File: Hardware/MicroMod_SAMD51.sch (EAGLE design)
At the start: 30 parts, among them J2 MICROMOD-2222, U1 W25QXX128MBIT-6X5-NO_CENTER, U2 ATSAMD51J20A-A, Y1 32.768kHz

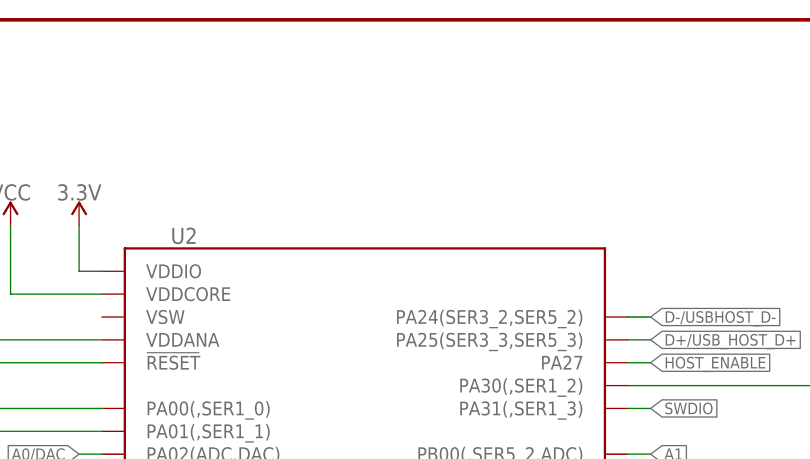
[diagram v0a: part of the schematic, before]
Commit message: Adds voltage range to schematic
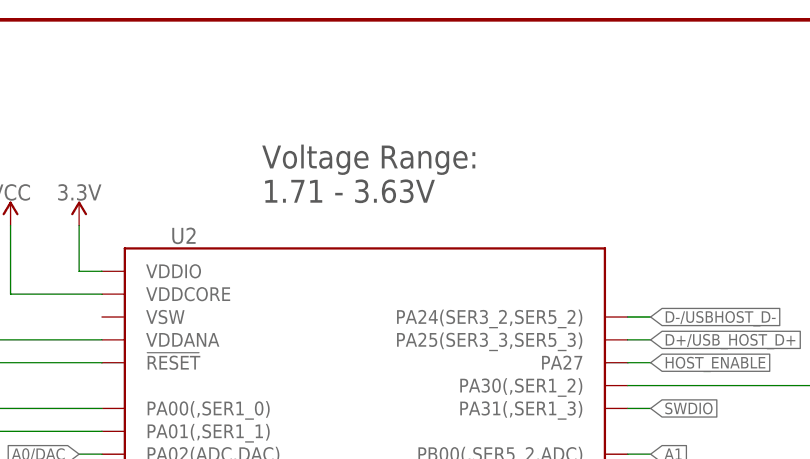
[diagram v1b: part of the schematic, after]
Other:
- note added: "Voltage Range: 1.71 - 3.63V"
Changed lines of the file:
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@@
 <text x="285.496" y="242.062" size="1.778" layer="97" font="vector">0.65uA Leakage
 0.3V drop at 10mA</text>
+<text x="106.68" y="259.08" size="2.54" layer="97" font="vector">Voltage Range:
+1.71 - 3.63V</text>
 </plain>
 <instances>

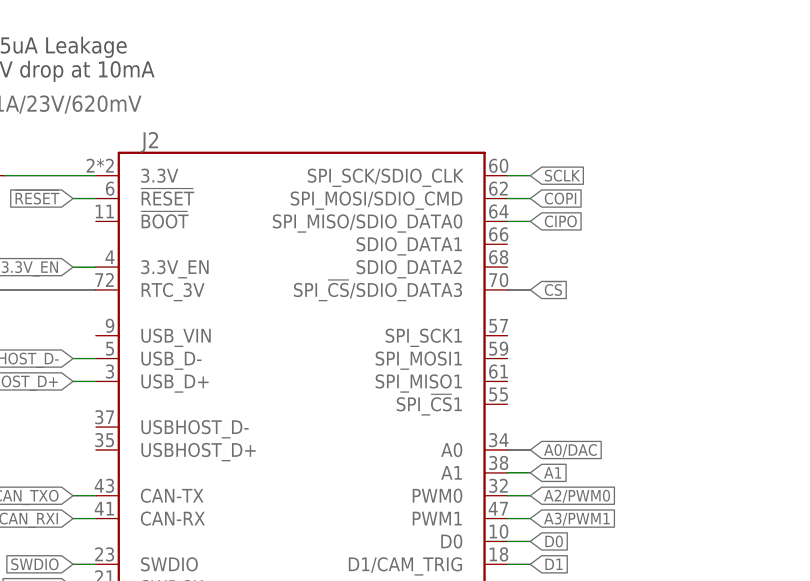
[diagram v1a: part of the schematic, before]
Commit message: Updates the micromodd connector and swaps the SPI pins
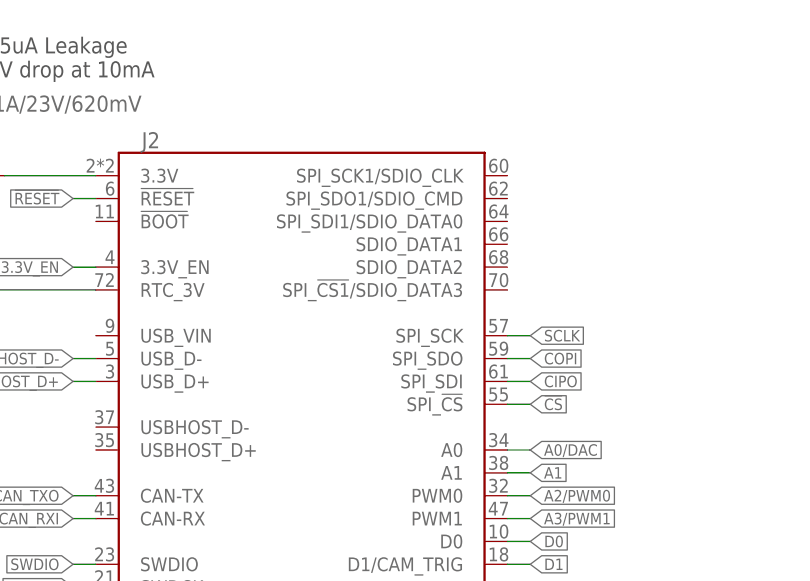
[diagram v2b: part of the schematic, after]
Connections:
- net !CS: now also J2.SPI_!CS!; no longer J2.SPI_!CS!/SDIO_DATA3
- net CIPO: now also J2.SPI_SDI; no longer J2.SPI_MISO/SDIO_DATA0
- net COPI: now also J2.SPI_SDO; no longer J2.SPI_MOSI/SDIO_CMD
- net SCLK: now also J2.SPI_SCK; no longer J2.SPI_SCK/SDIO_CLK
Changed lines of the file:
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@@
 </segment>
 <segment>
-<pinref part="J2" gate="J1" pin="SPI_MOSI/SDIO_CMD"/>
-<wire x1="345.44" y1="228.6" x2="347.98" y2="228.6" width="0.1524" layer="91"/>
-<label x="347.98" y="228.6" size="1.27" layer="95" xref="yes"/>
+<pinref part="J2" gate="J1" pin="SPI_SDO"/>
+<wire x1="345.44" y1="210.82" x2="347.98" y2="210.82" width="0.1524" layer="91"/>
+<label x="347.98" y="210.82" size="1.27" layer="95" xref="yes"/>
 </segment>
 </net>
 <net name="CIPO" class="0">
 <segment>
-<pinref part="J2" gate="J1" pin="SPI_MISO/SDIO_DATA0"/>
-<wire x1="345.44" y1="226.06" x2="347.98" y2="226.06" width="0.1524" layer="91"/>
-<label x="347.98" y="226.06" size="1.27" layer="95" xref="yes"/>
-</segment>
-<segment>
 <wire x1="88.9" y1="220.98" x2="86.36" y2="220.98" width="0.1524" layer="91"/>
 <label x="86.36" y="220.98" size="1.27" layer="95" font="vector" rot="R180" xref="yes"/>
 <pinref part="U2" gate="G$1" pin="PA06(,SER0_2,ADC,VREFC)"/>
+</segment>
+<segment>
+<pinref part="J2" gate="J1" pin="SPI_SDI"/>
+<wire x1="345.44" y1="208.28" x2="347.98" y2="208.28" width="0.1524" layer="91"/>
+<label x="347.98" y="208.28" size="1.27" layer="95" xref="yes"/>
 </segment>
 </net>
@@
 <net name="SCLK" class="1">
 <segment>
-<pinref part="J2" gate="J1" pin="SPI_SCK/SDIO_CLK"/>
-<wire x1="345.44" y1="231.14" x2="347.98" y2="231.14" width="0.1524" layer="91"/>
-<label x="347.98" y="231.14" size="1.27" layer="95" xref="yes"/>
-</segment>
-<segment>
 <wire x1="88.9" y1="223.52" x2="86.36" y2="223.52" width="0.1524" layer="91"/>
 <label x="86.36" y="223.52" size="1.27" layer="95" font="vector" rot="R180" xref="yes"/>
 <pinref part="U2" gate="G$1" pin="PA05(,SER0_1,ADC,DAC)"/>
+</segment>
+<segment>
+<pinref part="J2" gate="J1" pin="SPI_SCK"/>
+<wire x1="345.44" y1="213.36" x2="347.98" y2="213.36" width="0.1524" layer="91"/>
+<label x="347.98" y="213.36" size="1.27" layer="95" xref="yes"/>
 </segment>
 </net>
@@
 </segment>
 <segment>
-<pinref part="J2" gate="J1" pin="SPI_!CS!/SDIO_DATA3"/>
-<wire x1="345.44" y1="218.44" x2="347.98" y2="218.44" width="0.1524" layer="91"/>
-<label x="347.98" y="218.44" size="1.27" layer="95" xref="yes"/>
+<pinref part="J2" gate="J1" pin="SPI_!CS!"/>
+<wire x1="345.44" y1="205.74" x2="347.98" y2="205.74" width="0.1524" layer="91"/>
+<label x="347.98" y="205.74" size="1.27" layer="95" xref="yes"/>
 </segment>
 </net>

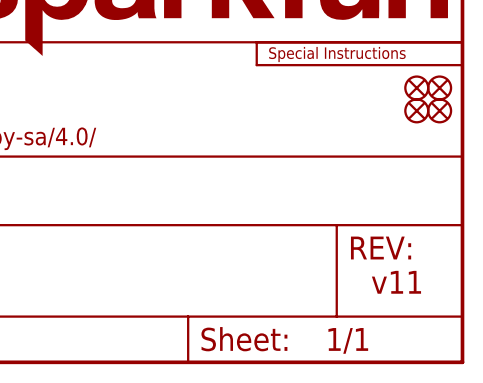
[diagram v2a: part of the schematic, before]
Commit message: Fixes LED assignment in variant,  routes SPI lines, rolls version to v12
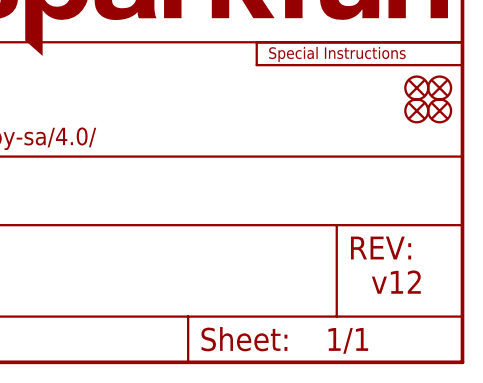
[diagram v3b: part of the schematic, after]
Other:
- note added: "v12"
- note removed: "v11"
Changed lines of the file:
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@@
 <sheet>
 <plain>
-<text x="421.64" y="7.62" size="2.54" layer="94" font="vector">v11</text>
+<text x="421.64" y="7.62" size="2.54" layer="94" font="vector">v12</text>
 <text x="250.64" y="273.78" size="2.54" layer="94" font="vector" align="center">M.2 Connector</text>
 <wire x1="231.14" y1="279.4" x2="231.14" y2="111.76" width="0.1524" layer="97" style="longdash"/>

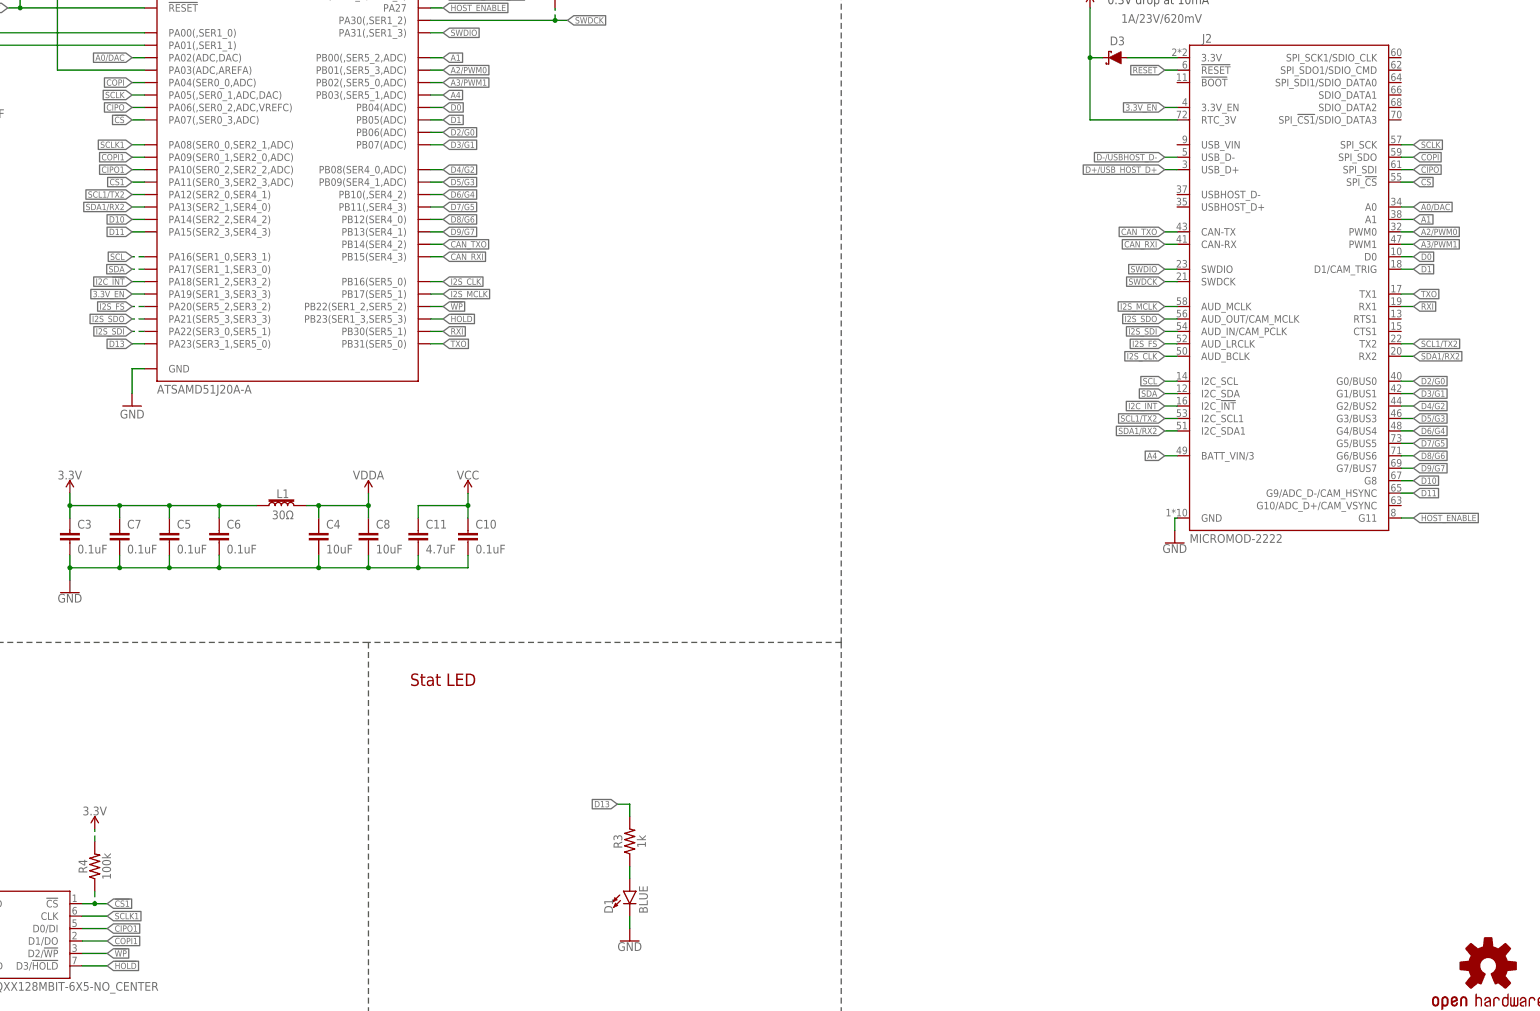
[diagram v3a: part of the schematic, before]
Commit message: Updates SPI clock names to correct abbreviation
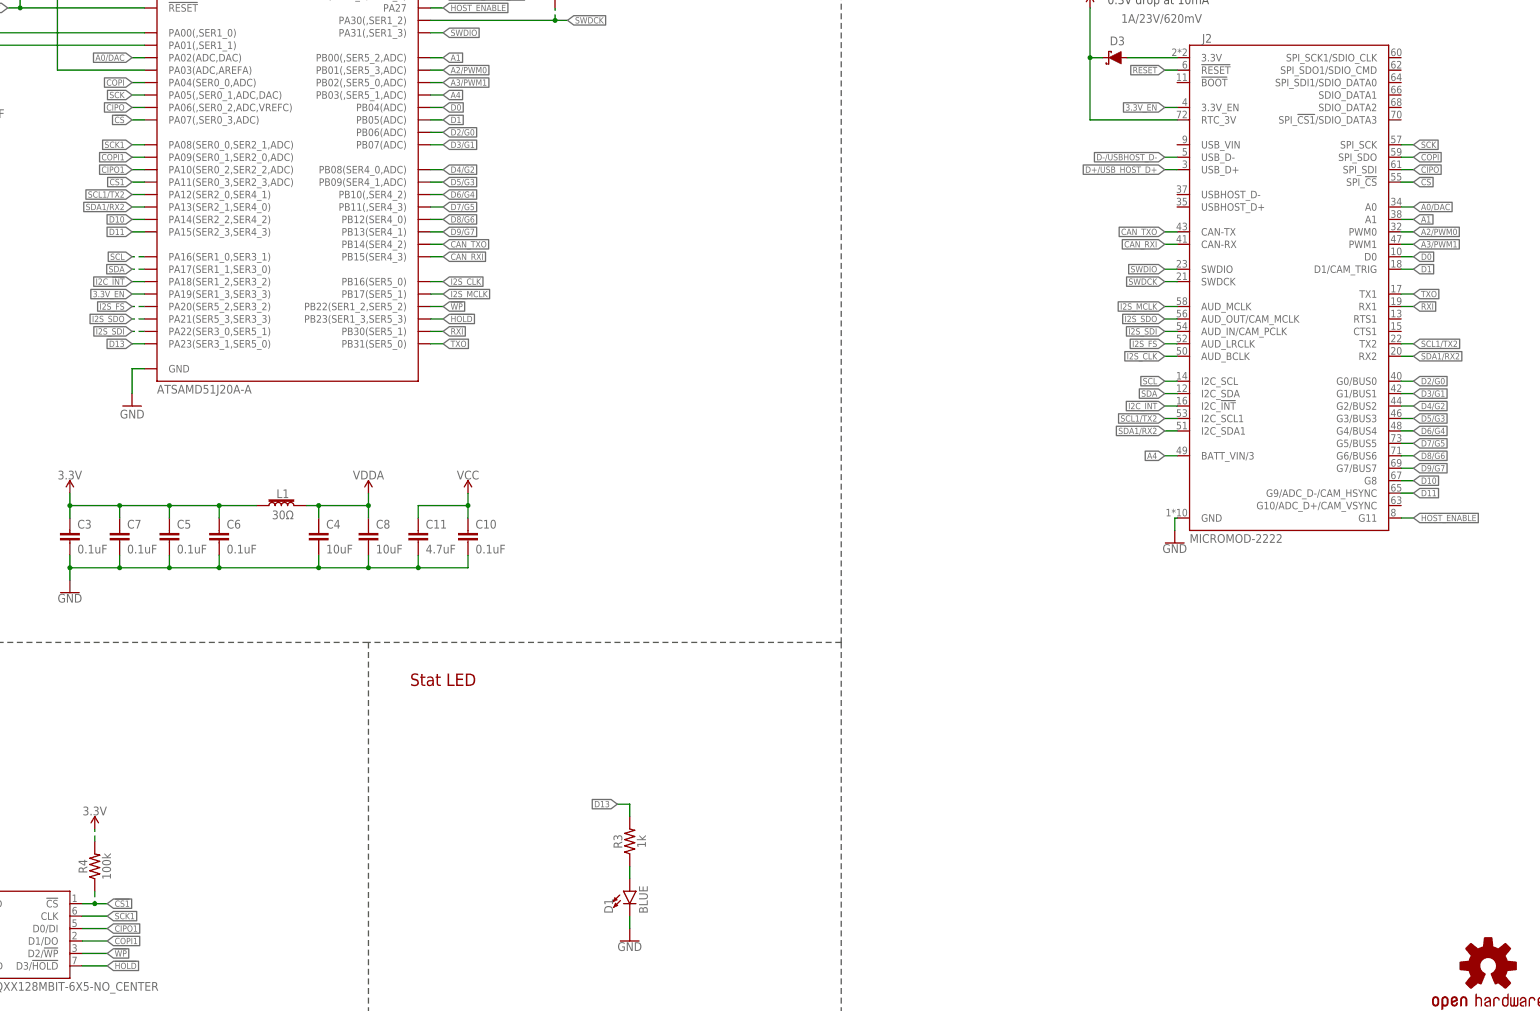
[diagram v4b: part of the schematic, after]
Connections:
- net SCLK renamed SCK
- net SCLK1 renamed SCK1
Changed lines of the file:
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@@
 </segment>
 </net>
-<net name="SCLK" class="1">
+<net name="SCK" class="1">
 <segment>
 <wire x1="88.9" y1="223.52" x2="86.36" y2="223.52" width="0.1524" layer="91"/>
@@
 </segment>
 </net>
-<net name="SCLK1" class="1">
+<net name="SCK1" class="1">
 <segment>
 <pinref part="U1" gate="U1" pin="CLK"/>

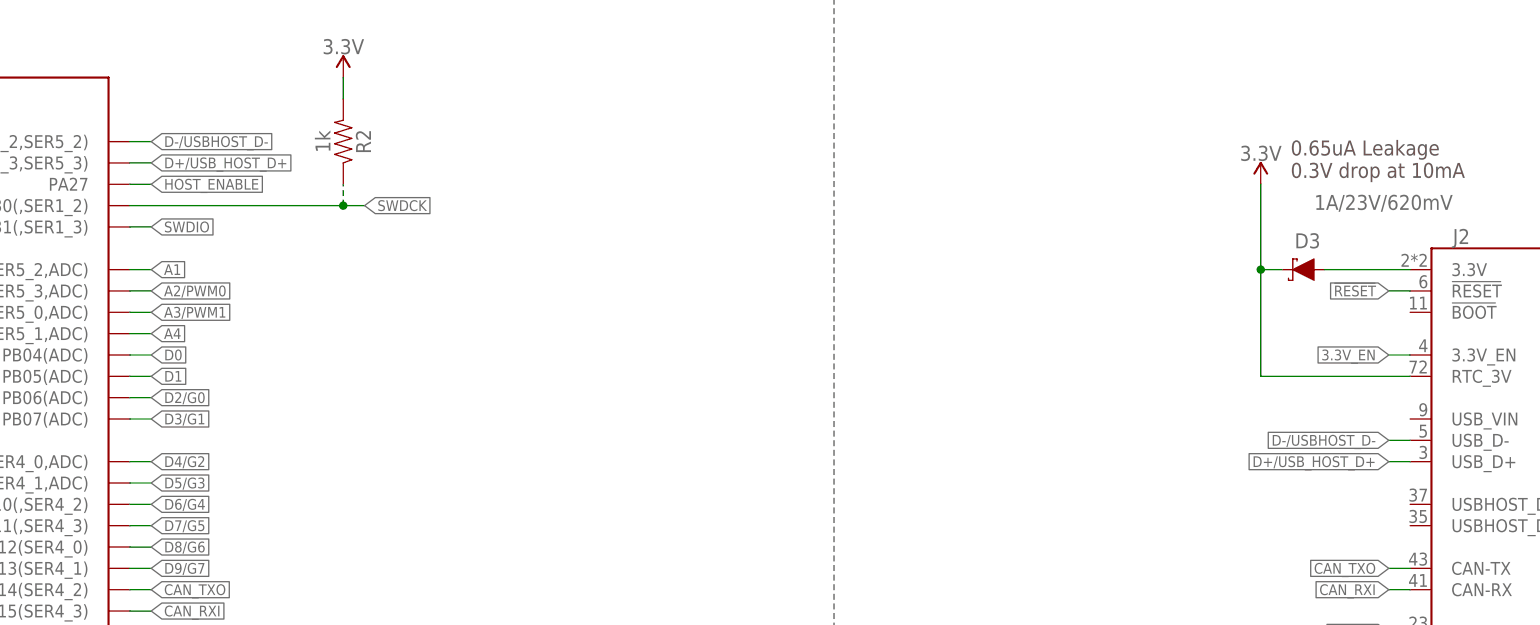
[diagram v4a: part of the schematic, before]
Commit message: Fixes typo in usbhost_D+ net
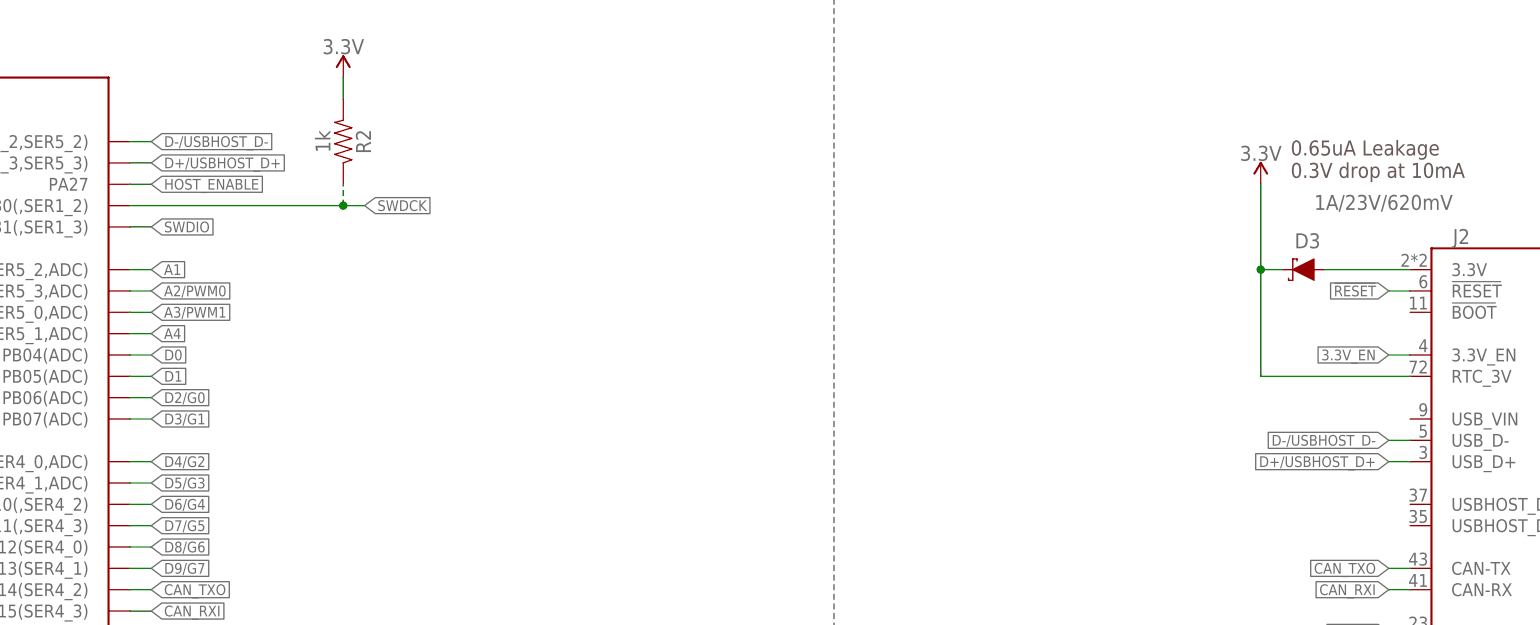
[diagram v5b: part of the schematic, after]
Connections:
- net D+/USB_HOST_D+ renamed D+/USBHOST_D+
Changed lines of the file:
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@@
 </segment>
 </net>
-<net name="D+/USB_HOST_D+" class="2">
+<net name="D+/USBHOST_D+" class="2">
 <segment>
 <pinref part="J2" gate="J1" pin="USB_D+"/>

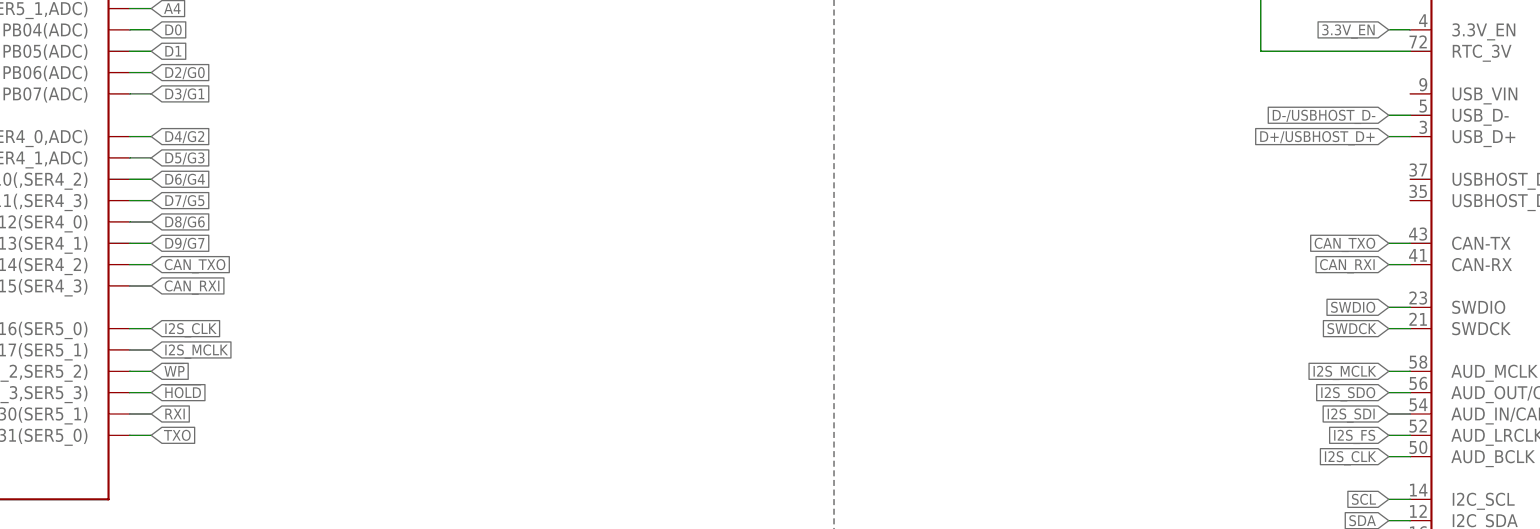
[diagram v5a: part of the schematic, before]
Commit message: Updates CAN net names - CAN is not supported on SAM-"D" versions of the IC
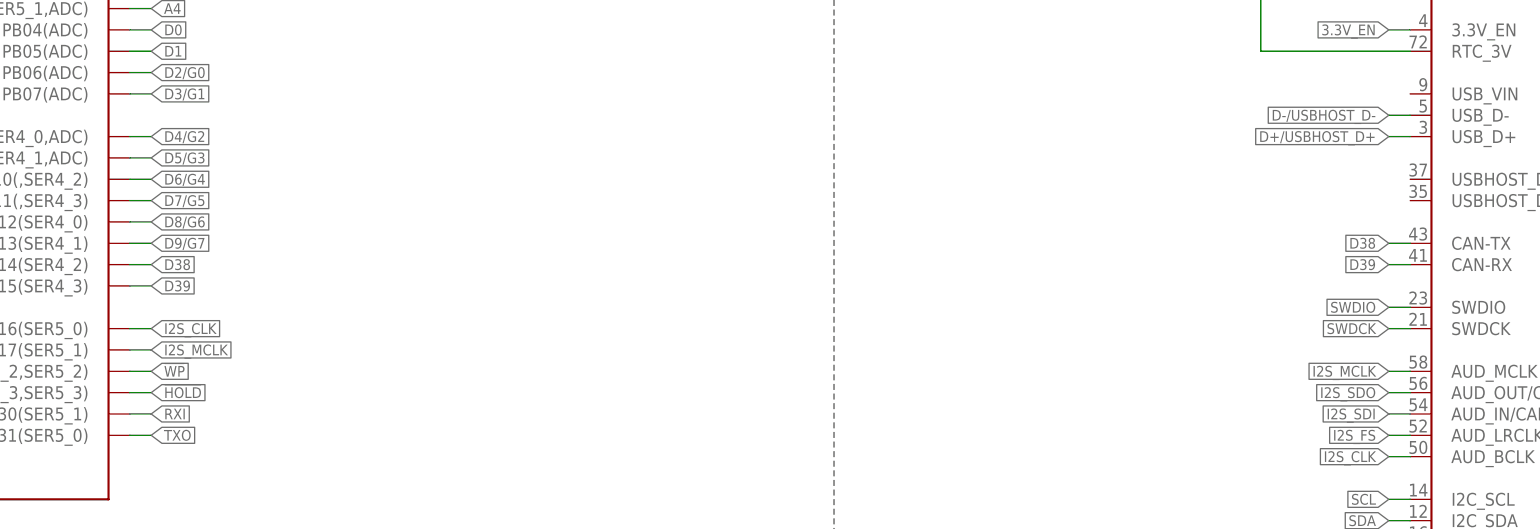
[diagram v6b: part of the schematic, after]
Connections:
- net CAN_RXI renamed D39
- net CAN_TXO renamed D38
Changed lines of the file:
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@@
 </segment>
 </net>
-<net name="CAN_TXO" class="0">
+<net name="D38" class="0">
 <segment>
 <wire x1="147.32" y1="193.04" x2="149.86" y2="193.04" width="0.1524" layer="91"/>
@@
 </segment>
 </net>
-<net name="CAN_RXI" class="0">
+<net name="D39" class="0">
 <segment>
 <wire x1="147.32" y1="190.5" x2="149.86" y2="190.5" width="0.1524" layer="91"/>
